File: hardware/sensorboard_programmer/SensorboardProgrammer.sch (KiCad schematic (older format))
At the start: 4 parts, among them P1 CONN_01X06, P2 CONN_01X06, SW1 SW_PUSH, SW2 SW_PUSH

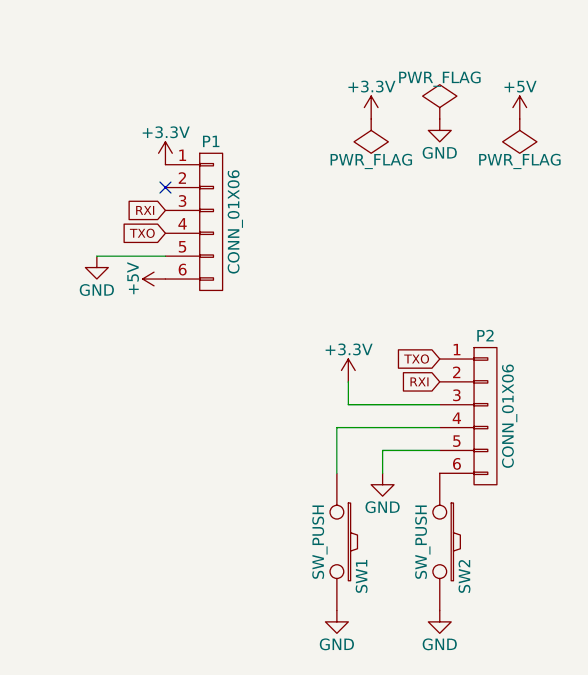
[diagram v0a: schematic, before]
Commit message: Better silkscreening and status LEDs.
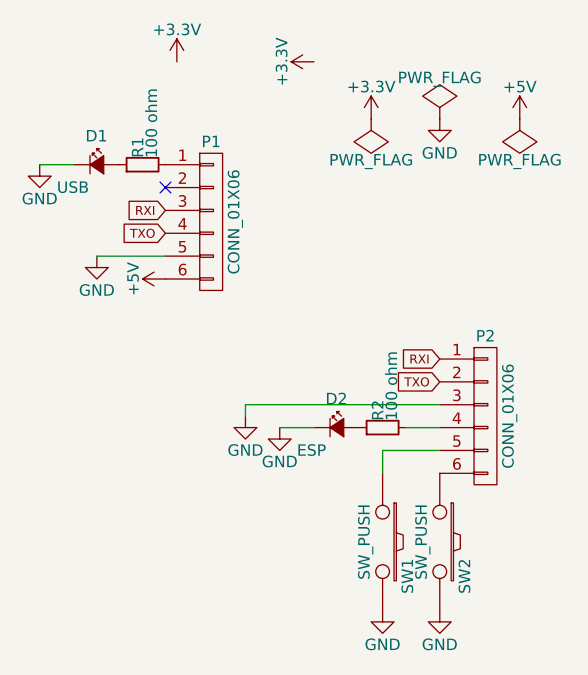
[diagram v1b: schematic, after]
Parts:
- added D1: USB, symbol Led_Small
- added D2: ESP, symbol Led_Small
- added R1, R2: 100 ohm, symbol R_Small
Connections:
- net +3V3: no longer P1.1 (P1), P2.3 (P3)
- net GND: now also P2.3 (P3), D1.1 (K), D2.1 (K); no longer P2.5 (P5)
- net RXI: now also P2.1 (P1); no longer P2.2 (P2)
- net TXO: now also P2.2 (P2); no longer P2.1 (P1)
- net at P2.4 (P4): now also R2.2; no longer SW1.1
- new net: P1.1 (P1), R1.2
- new net: P2.5 (P5), SW1.1
- new net: D1.2 (A), R1.1
- new net: D2.2 (A), R2.1
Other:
- moved on the sheet: SW1
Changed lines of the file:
@@
 LIBS:contrib
 LIBS:valves
-LIBS:Untitled-cache
+LIBS:SensorboardProgrammer-cache
 EELAYER 25 0
 EELAYER END
@@
 L +3.3V #PWR01
 U 1 1 56224BD5
-P 1150 1550
-F 0 "#PWR01" H 1150 1400 50  0001 C CNN
-F 1 "+3.3V" H 1150 1690 50  0000 C CNN
-F 2 "" H 1150 1550 60  0000 C CNN
-F 3 "" H 1150 1550 60  0000 C CNN
-	1    1150 1550
+P 1200 1100
+F 0 "#PWR01" H 1200 950 50  0001 C CNN
+F 1 "+3.3V" H 1200 1240 50  0000 C CNN
+F 2 "" H 1200 1100 60  0000 C CNN
+F 3 "" H 1200 1100 60  0000 C CNN
+	1    1200 1100
 	1    0    0    -1
 $EndComp
@@
 L SW_PUSH SW1
 U 1 1 56224D59
-P 1900 3200
-F 0 "SW1" H 2050 3310 50  0000 C CNN
-F 1 "SW_PUSH" H 1900 3120 50  0000 C CNN
-F 2 "Buttons_Switches_ThroughHole:SW_PUSH_SMALL" H 1900 3200 60  0001 C CNN
-F 3 "" H 1900 3200 60  0000 C CNN
-	1    1900 3200
+P 2100 3200
+F 0 "SW1" H 2250 3310 50  0000 C CNN
+F 1 "SW_PUSH" H 2100 3120 50  0000 C CNN
+F 2 "Buttons_Switches_ThroughHole:SW_PUSH_SMALL" H 2100 3200 60  0001 C CNN
+F 3 "" H 2100 3200 60  0000 C CNN
+	1    2100 3200
 	0    1    1    0
 $EndComp
@@
 L GND #PWR04
 U 1 1 562254B3
-P 1900 3500
-F 0 "#PWR04" H 1900 3250 50  0001 C CNN
-F 1 "GND" H 1900 3350 50  0000 C CNN
-F 2 "" H 1900 3500 60  0000 C CNN
-F 3 "" H 1900 3500 60  0000 C CNN
-	1    1900 3500
+P 2100 3500
+F 0 "#PWR04" H 2100 3250 50  0001 C CNN
+F 1 "GND" H 2100 3350 50  0000 C CNN
+F 2 "" H 2100 3500 60  0000 C CNN
+F 3 "" H 2100 3500 60  0000 C CNN
+	1    2100 3500
 	1    0    0    -1
 $EndComp
@@
 L GND #PWR06
 U 1 1 562254E9
-P 2100 2900
-F 0 "#PWR06" H 2100 2650 50  0001 C CNN
-F 1 "GND" H 2100 2750 50  0000 C CNN
-F 2 "" H 2100 2900 60  0000 C CNN
-F 3 "" H 2100 2900 60  0000 C CNN
-	1    2100 2900
-	1    0    0    -1
-$EndComp
+P 1500 2650
+F 0 "#PWR06" H 1500 2400 50  0001 C CNN
+F 1 "GND" H 1500 2500 50  0000 C CNN
+F 2 "" H 1500 2650 60  0000 C CNN
+F 3 "" H 1500 2650 60  0000 C CNN
+	1    1500 2650
+	1    0    0    -1
+$EndComp
+Text GLabel 2350 2400 0    39   Input ~ 0
+RXI
 Text GLabel 2350 2500 0    39   Input ~ 0
-RXI
-Text GLabel 2350 2400 0    39   Input ~ 0
 TXO
 $Comp
 L +3.3V #PWR07
 U 1 1 5622555D
-P 1950 2500
-F 0 "#PWR07" H 1950 2350 50  0001 C CNN
-F 1 "+3.3V" H 1950 2640 50  0000 C CNN
-F 2 "" H 1950 2500 60  0000 C CNN
-F 3 "" H 1950 2500 60  0000 C CNN
-	1    1950 2500
-	1    0    0    -1
+P 1800 1100
+F 0 "#PWR07" H 1800 950 50  0001 C CNN
+F 1 "+3.3V" H 1800 1240 50  0000 C CNN
+F 2 "" H 1800 1100 60  0000 C CNN
+F 3 "" H 1800 1100 60  0000 C CNN
+	1    1800 1100
+	0    -1   -1   0
 $EndComp
 Wire Wire Line
 	850  1950 1150 1950
 Wire Wire Line
-	2350 2700 1900 2700
-Wire Wire Line
-	1900 2700 1900 2900
-Wire Wire Line
 	2100 2900 2100 2800
 Wire Wire Line
 	2100 2800 2350 2800
-Wire Wire Line
-	1950 2500 1950 2600
-Wire Wire Line
-	1950 2600 2350 2600
 NoConn ~ 1150 1650
 $Comp
@@
 	-1   0    0    1
 $EndComp
+Wire Wire Line
+	1500 2600 2350 2600
+Wire Wire Line
+	2200 2700 2350 2700
+$Comp
+L R_Small R1
+U 1 1 56397FCC
+P 1050 1550
+F 0 "R1" H 1080 1570 50  0000 L CNN
+F 1 "100 ohm" H 1080 1510 50  0000 L CNN
+F 2 "" H 1050 1550 60  0000 C CNN
+F 3 "" H 1050 1550 60  0000 C CNN
+	1    1050 1550
+	0    -1   -1   0
+$EndComp
+$Comp
+L R_Small R2
+U 1 1 5639801C
+P 2100 2700
+F 0 "R2" H 2130 2720 50  0000 L CNN
+F 1 "100 ohm" H 2130 2660 50  0000 L CNN
+F 2 "" H 2100 2700 60  0000 C CNN
+F 3 "" H 2100 2700 60  0000 C CNN
+	1    2100 2700
+	0    -1   -1   0
+$EndComp
+$Comp
+L Led_Small D1
+U 1 1 563980D8
+P 850 1550
+F 0 "D1" H 800 1675 50  0000 L CNN
+F 1 "USB" H 675 1450 50  0000 L CNN
+F 2 "" V 850 1550 60  0000 C CNN
+F 3 "" V 850 1550 60  0000 C CNN
+	1    850  1550
+	1    0    0    -1
+$EndComp
+$Comp
+L GND #PWR?
+U 1 1 56398115
+P 600 1550
+F 0 "#PWR?" H 600 1300 50  0001 C CNN
+F 1 "GND" H 600 1400 50  0000 C CNN
+F 2 "" H 600 1550 60  0000 C CNN
+F 3 "" H 600 1550 60  0000 C CNN
+	1    600  1550
+	1    0    0    -1
+$EndComp
+Wire Wire Line
+	600  1550 750  1550
+$Comp
+L Led_Small D2
+U 1 1 56398144
+P 1900 2700
+F 0 "D2" H 1850 2825 50  0000 L CNN
+F 1 "ESP" H 1725 2600 50  0000 L CNN
+F 2 "" V 1900 2700 60  0000 C CNN
+F 3 "" V 1900 2700 60  0000 C CNN
+	1    1900 2700
+	1    0    0    -1
+$EndComp
+Wire Wire Line
+	1500 2600 1500 2650
+$Comp
+L GND #PWR?
+U 1 1 563981C6
+P 1650 2700
+F 0 "#PWR?" H 1650 2450 50  0001 C CNN
+F 1 "GND" H 1650 2550 50  0000 C CNN
+F 2 "" H 1650 2700 60  0000 C CNN
+F 3 "" H 1650 2700 60  0000 C CNN
+	1    1650 2700
+	1    0    0    -1
+$EndComp
+Wire Wire Line
+	1800 2700 1650 2700
 $EndSCHEMATC

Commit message: Add LEDs and improved silkscreens.
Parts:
- D1, D2: footprint (none) -> LEDs:LED-0805
- R1, R2: footprint (none) -> Resistors_SMD:R_0603_HandSoldering
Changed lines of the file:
@@
 F 0 "R1" H 1080 1570 50  0000 L CNN
 F 1 "100 ohm" H 1080 1510 50  0000 L CNN
-F 2 "" H 1050 1550 60  0000 C CNN
+F 2 "Resistors_SMD:R_0603_HandSoldering" H 1050 1550 60  0001 C CNN
 F 3 "" H 1050 1550 60  0000 C CNN
 	1    1050 1550
@@
 F 0 "R2" H 2130 2720 50  0000 L CNN
 F 1 "100 ohm" H 2130 2660 50  0000 L CNN
-F 2 "" H 2100 2700 60  0000 C CNN
+F 2 "Resistors_SMD:R_0603_HandSoldering" H 2100 2700 60  0001 C CNN
 F 3 "" H 2100 2700 60  0000 C CNN
 	1    2100 2700
@@
 F 0 "D1" H 800 1675 50  0000 L CNN
 F 1 "USB" H 675 1450 50  0000 L CNN
-F 2 "" V 850 1550 60  0000 C CNN
+F 2 "LEDs:LED-0805" V 850 1550 60  0001 C CNN
 F 3 "" V 850 1550 60  0000 C CNN
 	1    850  1550
@@
 $EndComp
 $Comp
-L GND #PWR?
+L GND #PWR014
 U 1 1 56398115
 P 600 1550
-F 0 "#PWR?" H 600 1300 50  0001 C CNN
+F 0 "#PWR014" H 600 1300 50  0001 C CNN
 F 1 "GND" H 600 1400 50  0000 C CNN
 F 2 "" H 600 1550 60  0000 C CNN
@@
 F 0 "D2" H 1850 2825 50  0000 L CNN
 F 1 "ESP" H 1725 2600 50  0000 L CNN
-F 2 "" V 1900 2700 60  0000 C CNN
+F 2 "LEDs:LED-0805" V 1900 2700 60  0001 C CNN
 F 3 "" V 1900 2700 60  0000 C CNN
 	1    1900 2700
@@
 	1500 2600 1500 2650
 $Comp
-L GND #PWR?
+L GND #PWR015
 U 1 1 563981C6
 P 1650 2700
-F 0 "#PWR?" H 1650 2450 50  0001 C CNN
+F 0 "#PWR015" H 1650 2450 50  0001 C CNN
 F 1 "GND" H 1650 2550 50  0000 C CNN
 F 2 "" H 1650 2700 60  0000 C CNN
